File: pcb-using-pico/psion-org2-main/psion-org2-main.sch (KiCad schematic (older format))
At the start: 57 parts, among them J1 Conn_01x24_Female, J2 Conn_01x03_Female, J3 Conn_01x27_Female, U1 Pico, U10 AMS1117-3.3, U11 AMS1117-3.3, U2 74HC595, U3 Regulator_Switching_MT3608, U4 74LS165, U5 MCP7940N-xSN, U6 74LS245, U7 74LS245, Y1 32k768Hz

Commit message: Updates to both PCBs
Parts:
- removed C13, C14: C, Capacitor_SMD:C_0805_2012Metric, symbol Device:C
- removed R14: 4k7, Resistor_SMD:R_0805_2012Metric, symbol Device:R_Small
- removed R15: R_Small, Resistor_SMD:R_0805_2012Metric, symbol Device:R_Small
- removed U5: MCP7940N-xSN, Package_SO:SO-8_3.9x4.9mm_P1.27mm, symbol Timer:MCP7940N-xSN
- removed U6, U7: 74LS245, Package_SO:TSSOP-20_4.4x6.5mm_P0.65mm, symbol 74xx:74LS245
- removed Y1: 32k768Hz, Crystal:Crystal_SMD_3215-2Pin_3.2x1.5mm, symbol Device:Crystal
- added C13: 1uF, Capacitor_SMD:C_0805_2012Metric, symbol Device:C_Small
- added J?: Conn_01x02_Female, symbol Connector:Conn_01x02_Female
- added TR2: Si2302CDS-n-channel, Package_TO_SOT_SMD:SOT-23, symbol New_Library:Si2302CDS-n-channel
- added U5: 74HC595, Package_SO:SOIC-16_3.9x9.9mm_P1.27mm, symbol 74xx:74HC595
- added U8: ESP32-WROOM-32, RF_Module:ESP32-WROOM-32, symbol RF_Module:ESP32-WROOM-32
- D1: footprint (none) -> Diode_SMD:D_SOD-123
- R13: value 4k7 -> 10k
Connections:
- net labels added: ESP_ON, LATCHOUT1, LATCHOUT2, PICO_RX, PICO_TX
- net labels removed: +3.3V, LATCHOUT, P_SS, RTC_MFP, RTC_SCL, RTC_SDA
- wire segments 292 -> 269
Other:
- note added: "P57 used for power on"
- note removed: "850nA 1300mV\n1200nA 3000mV\n9000nA 5500mV\n"
- note removed: "KR0 used for power on"
- moved on the sheet: R22, R23

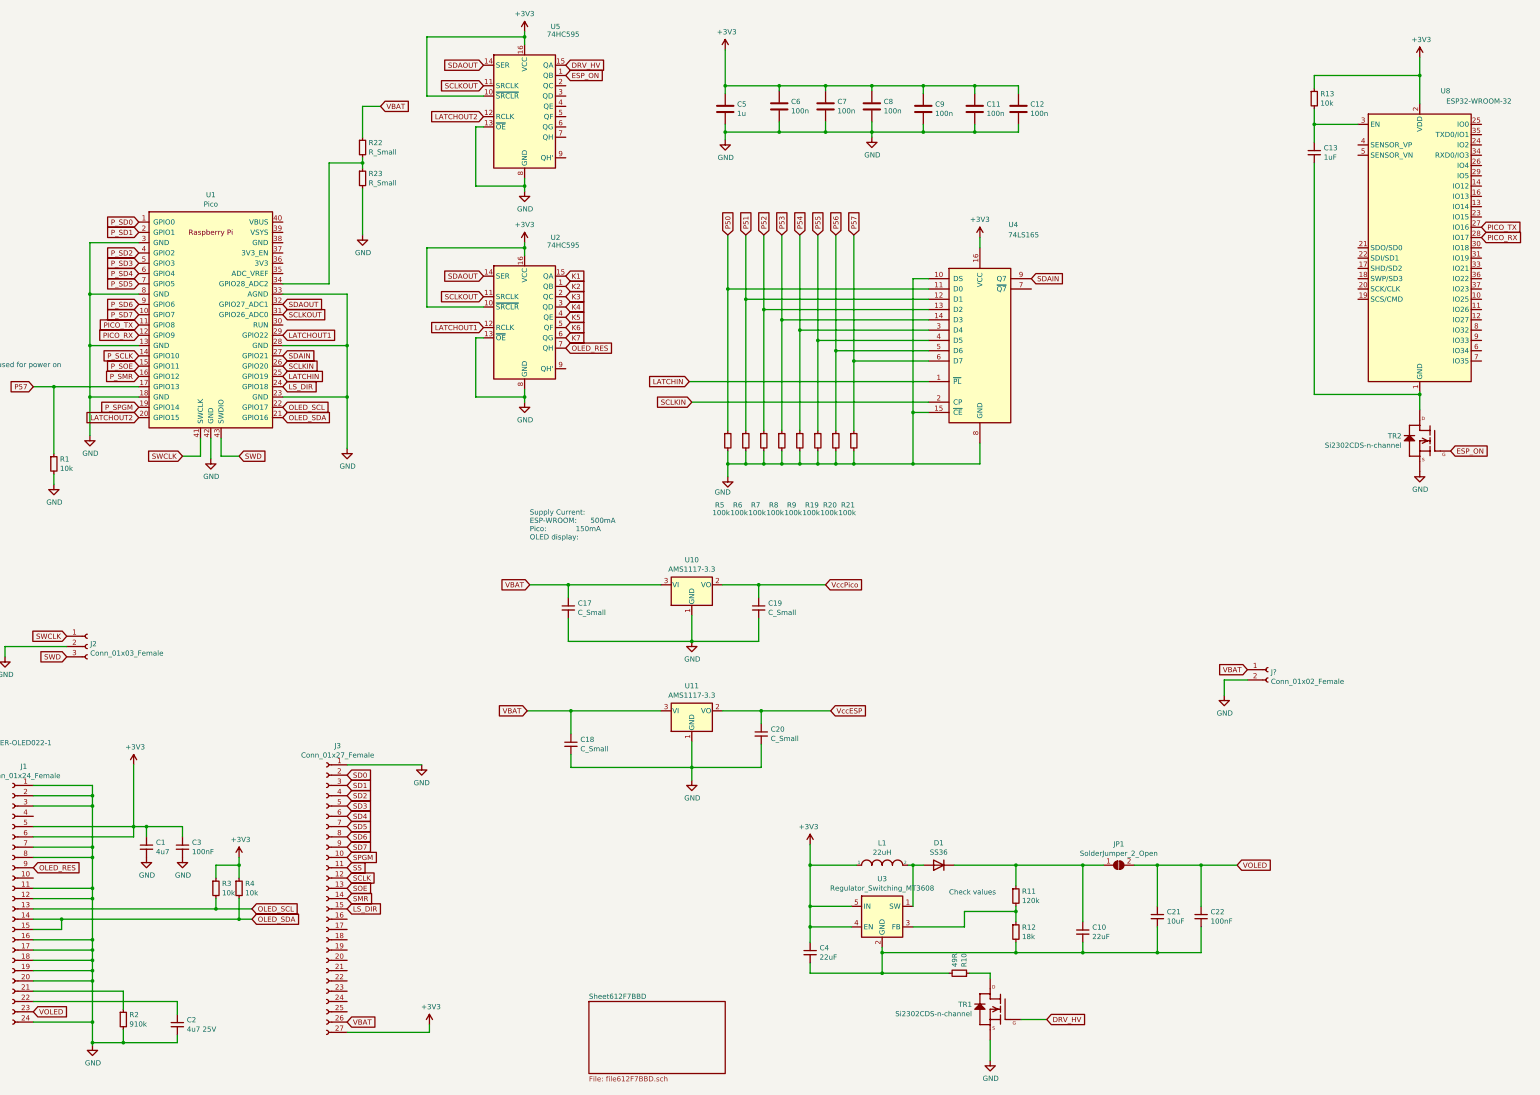
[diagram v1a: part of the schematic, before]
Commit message: Added second connector, eeprom on power pcb
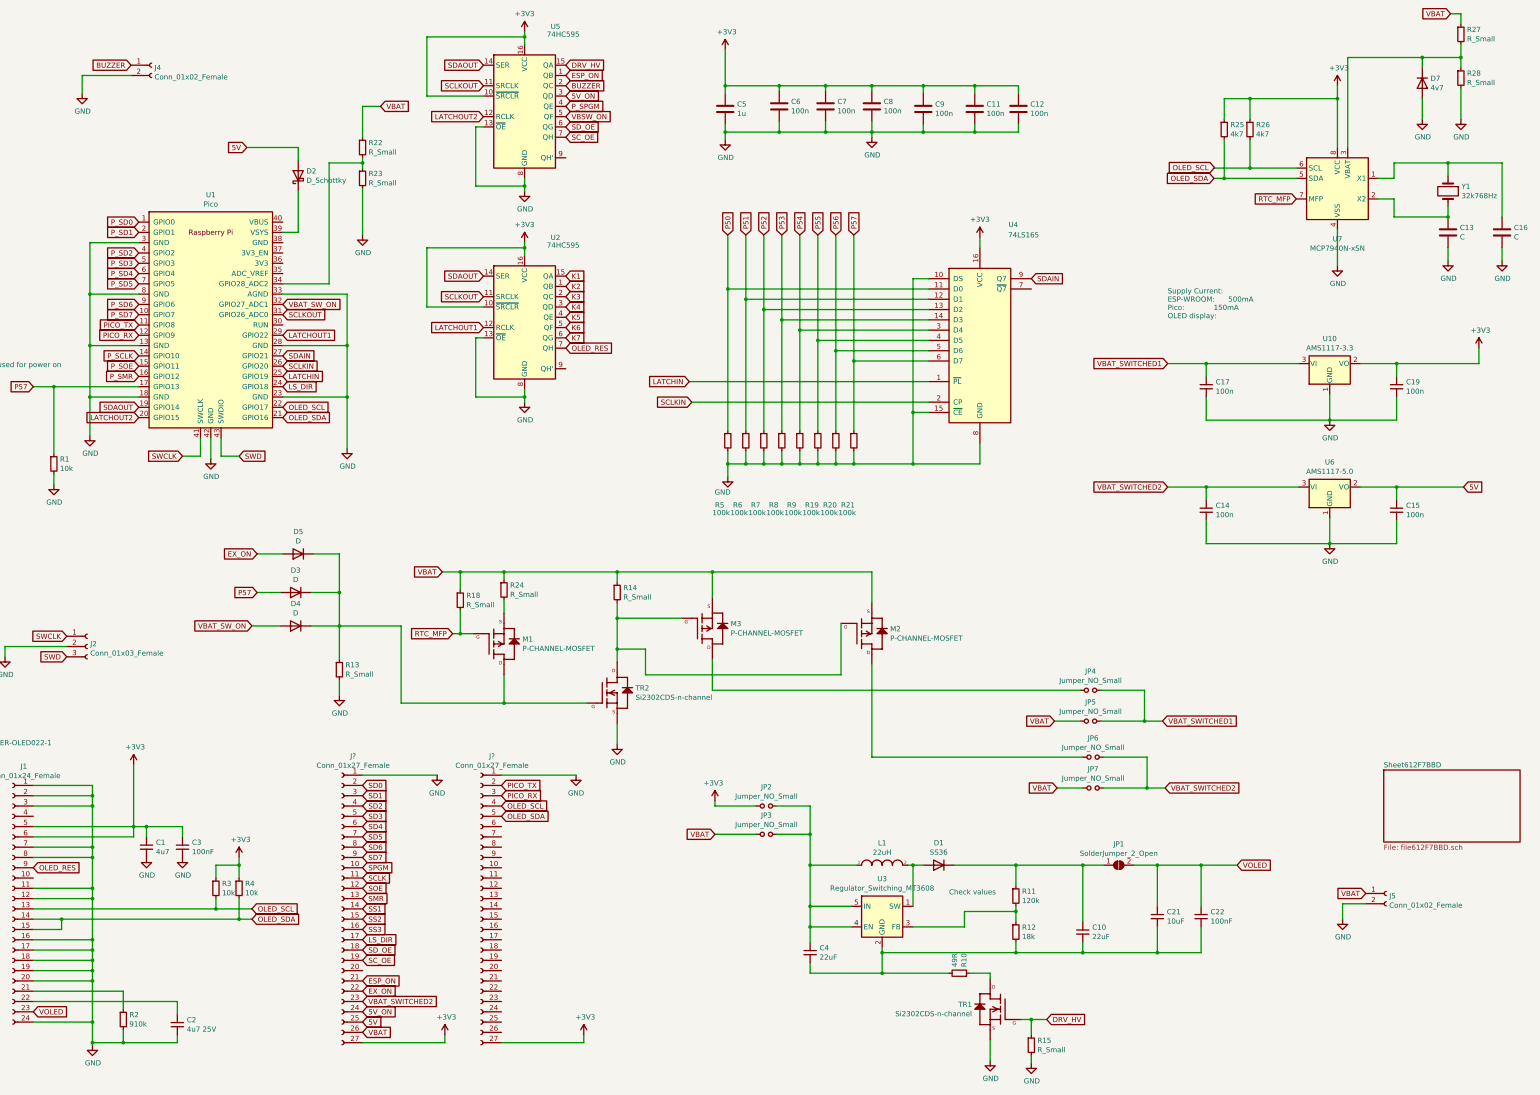
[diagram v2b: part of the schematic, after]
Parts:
- removed C13: 1uF, Capacitor_SMD:C_0805_2012Metric, symbol Device:C_Small
- removed C18, C20: C_Small, Capacitor_SMD:C_0805_2012Metric, symbol Device:C_Small
- removed J3: Conn_01x27_Female, Connector_PinHeader_2.54mm:PinHeader_1x27_P2.54mm_Vertical, symbol Connector:Conn_01x27_Female
- removed U11: AMS1117-3.3, Package_TO_SOT_SMD:SOT-223-3_TabPin2, symbol pak_breakout:AMS1117-3.3
- removed U8: ESP32-WROOM-32, RF_Module:ESP32-WROOM-32, symbol RF_Module:ESP32-WROOM-32
- added C13, C16: C, Capacitor_SMD:C_0805_2012Metric, symbol Device:C
- added C14, C15: 100n, Capacitor_SMD:C_0805_2012Metric, symbol Device:C_Small
- added D2: D_Schottky, Diode_SMD:D_SOD-123, symbol Device:D_Schottky
- added D3, D4, D5: D, Diode_SMD:D_SOD-123, symbol Device:D
- added D7: 4v7, Diode_SMD:D_SOD-123, symbol Device:D
- added J4: Conn_01x02_Female, Connector_PinHeader_2.54mm:PinHeader_1x02_P2.54mm_Vertical_SMD_Pin1Left, symbol Connector:Conn_01x02_Female
- added J? (x2): Conn_01x27_Female, Connector_PinHeader_2.54mm:PinHeader_1x27_P2.54mm_Vertical, symbol Connector:Conn_01x27_Female
- added JP2, JP3, JP4, JP5, JP6, JP7: Jumper_NO_Small, Jumper:SolderJumper-2_P1.3mm_Open_RoundedPad1.0x1.5mm, symbol Device:Jumper_NO_Small
- added M1, M2, M3: P-CHANNEL-MOSFET, Package_TO_SOT_SMD:SOT-23, symbol GeekAmmo:P-CHANNEL-MOSFET
- added R14, R15, R18, R24, R27, R28: R_Small, Resistor_SMD:R_0805_2012Metric, symbol Device:R_Small
- added R25, R26: 4k7, Resistor_SMD:R_0805_2012Metric, symbol Device:R_Small
- added U6: AMS1117-5.0, Package_TO_SOT_SMD:SOT-223-3_TabPin2, symbol pak_breakout:AMS1117-5.0
- added U7: MCP7940N-xSN, Package_SO:SO-8_3.9x4.9mm_P1.27mm, symbol Timer:MCP7940N-xSN
- added Y1: 32k768Hz, Crystal:Crystal_SMD_3215-2Pin_3.2x1.5mm, symbol Device:Crystal
- C17, C19: value C_Small -> 100n
- J5: renamed from J?; footprint (none) -> Connector_PinHeader_2.54mm:PinHeader_1x02_P2.54mm_Vertical_SMD_Pin1Left
- R13: value 10k -> R_Small
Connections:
- net VccPico is gone; now on net +3V3: C19.1, U10.2 (VO)
- net +3V3: now also J?.27 (Pin_27), J?.27 (Pin_27), JP2.1, R25.1, R26.1, U7.8 (VCC); no longer C4.1, L1.1, R13.1, U3.4 (EN), U3.5 (IN)
- net DRV_HV: now also R15.1
- net ESP_ON: now also J?.21 (Pin_21); no longer TR2.1 (G)
- net GND: now also R13.2, C13.2, C14.2, C15.2, C16.2, D7.2 (A), J4.2 (Pin_2), J?.1 (Pin_1), J?.1 (Pin_1), R15.2, R28.2, U6.1 (GND), U7.4 (VSS)
- net LS_DIR: now also J?.17 (Pin_17)
- net OLED_SCL: now also J?.4 (Pin_4), R26.2, U7.6 (SCL)
- net OLED_SDA: now also J?.5 (Pin_5), R25.2, U7.5 (SDA)
- net P57: now also D3.2 (A)
- net PICO_RX: now also J?.3 (Pin_3)
- net PICO_TX: now also J?.2 (Pin_2)
- net P_SPGM: now also U5.4 (QE); no longer U1.19 (GPIO14)
- net SCLK: now also J?.11 (Pin_11)
- net SD0: now also J?.2 (Pin_2)
- net SD1: now also J?.3 (Pin_3)
- net SD2: now also J?.4 (Pin_4)
- net SD3: now also J?.5 (Pin_5)
- net SD4: now also J?.6 (Pin_6)
- net SD5: now also J?.7 (Pin_7)
- net SD6: now also J?.8 (Pin_8)
- net SD7: now also J?.9 (Pin_9)
- net SDAOUT: now also U1.19 (GPIO14); no longer U1.32 (GPIO27_ADC1)
- net SMR: now also J?.13 (Pin_13)
- net SOE: now also J?.12 (Pin_12)
- net SPGM: now also J?.10 (Pin_10)
- net VBAT: now also J?.26 (Pin_26), JP3.1, JP5.1, JP7.1, M2.2 (S), M3.2 (S), R14.1, R18.1, R24.1, R27.1; no longer C17.1, U10.3 (VI)
- net at U1.39 (VSYS): now also D2.1 (K)
- net BUZZER: now reaches U5.2 (QC)
- net BUZZER: now also J4.1 (Pin_1)
- net 5V_ON: now reaches U5.3 (QD)
- net 5V_ON: now also J?.24 (Pin_24)
- net VBSW_ON: now reaches U5.5 (QF)
- net SD_OE: now reaches U5.6 (QG)
- net SD_OE: now also J?.18 (Pin_18)
- net SC_OE: now reaches U5.7 (QH)
- net SC_OE: now also J?.19 (Pin_19)
- net at TR2.3 (D): now also M2.1 (G), M3.1 (G), R14.2
- new net: C4.1, JP2.2, JP3.2, L1.1, U3.4 (EN), U3.5 (IN)
- new net: D3.1 (K), D4.1 (K), D5.1 (K), M1.3 (D), R13.1, TR2.1 (G)
- new net: M1.2 (S), R24.2
- new net: JP4.1, M3.3 (D)
- new net: JP6.1, M2.3 (D)
- new net: C16.1, U7.1 (X1), Y1.1
- new net: C13.1, U7.2 (X2), Y1.2
- new net: D7.1 (K), R27.2, R28.1, U7.3 (VBAT)
- new net 5V: C15.1, D2.2 (A), J?.25 (Pin_25), U6.2 (VO)
- new net EX_ON: D5.2 (A), J?.22 (Pin_22)
- new net RTC_MFP: M1.1 (G), R18.2, U7.7 (MFP)
- new net SS1: J?.14 (Pin_14)
- new net SS2: J?.15 (Pin_15)
- new net SS3: J?.16 (Pin_16)
- new net VBAT_SWITCHED1: C17.1, JP4.2, JP5.2, U10.3 (VI)
- new net VBAT_SWITCHED2: C14.1, J?.23 (Pin_23), JP6.2, JP7.2, U6.3 (VI)
- new net VBAT_SW_ON: D4.2 (A), U1.32 (GPIO27_ADC1)
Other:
- moved on the sheet: C17, C19, J5, U10
